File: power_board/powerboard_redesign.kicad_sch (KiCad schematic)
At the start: 18 parts, among them J1 282834-2, J2 282834-2, J3 282834-2, J4 282834-2, J5 BM06B-SRSS-TBLFSN, U1 PDQ30-Q24-D12-D

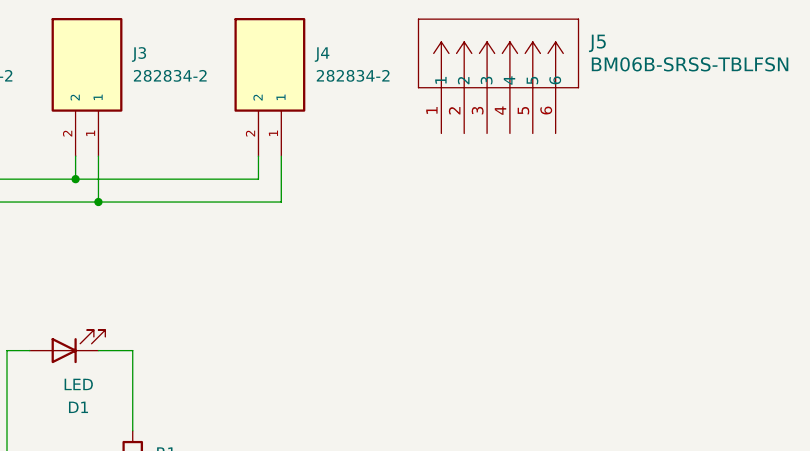
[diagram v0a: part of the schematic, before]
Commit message: Added connections to BM06B-SRSS-TB
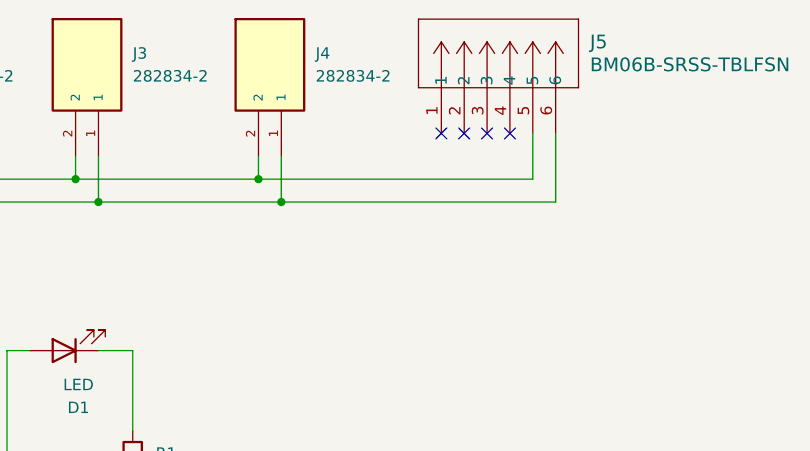
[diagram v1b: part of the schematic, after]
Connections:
- net at J5.5: now also C1.1, C4.1, C5.1, D1.2 (A), J2.2, J3.2, J4.2, U1.3 (+VOUT)
- net at J5.6: now also C1.2, C4.2, C5.2, J2.1, J3.1, J4.1, R1.2, U1.4 (COMMON)
- no-connect marks 3 -> 7
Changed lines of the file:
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@@
+	)
+	(junction
+		(at 223.52 58.42)
+		(diameter 0)
+		(color 0 0 0 0)
 	)
 	(junction
@@
 	)
 	(junction
+		(at 220.98 55.88)
+		(diameter 0)
+		(color 0 0 0 0)
+	)
+	(junction
 		(at 157.48 81.28)
 		(diameter 0)
@@
 	)
 	(no_connect
+		(at 246.38 50.8)
+	)
+	(no_connect
 		(at 157.48 93.98)
 	)
 	(no_connect
+		(at 248.92 50.8)
+	)
+	(no_connect
+		(at 241.3 50.8)
+	)
+	(no_connect
 		(at 83.82 86.36)
 	)
@@
 		(at 121.92 99.06)
 	)
+	(no_connect
+		(at 243.84 50.8)
+	)
 	(wire
 		(pts
@@
 	(wire
 		(pts
+			(xy 254 50.8) (xy 254 58.42)
+		)
+		(stroke
+			(width 0)
+			(type default)
+		)
+	)
+	(wire
+		(pts
+			(xy 223.52 58.42) (xy 254 58.42)
+		)
+		(stroke
+			(width 0)
+			(type default)
+		)
+	)
+	(wire
+		(pts
 			(xy 121.92 93.98) (xy 120.65 93.98)
 		)
@@
 	(wire
 		(pts
+			(xy 220.98 55.88) (xy 251.46 55.88)
+		)
+		(stroke
+			(width 0)
+			(type default)
+		)
+	)
+	(wire
+		(pts
 			(xy 203.2 53.34) (xy 203.2 58.42)
 		)
@@
 		)
 		(stroke
+			(width 0)
+			(type default)
+		)
+	)
+	(wire
+		(pts
+			(xy 251.46 50.8) (xy 251.46 55.88)
+		)
+		(stroke

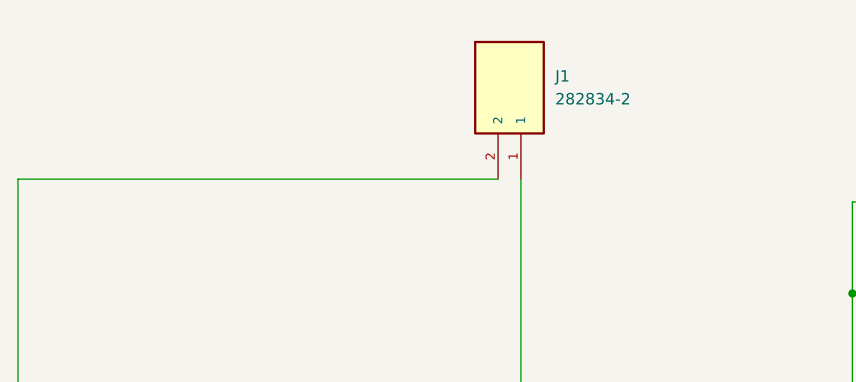
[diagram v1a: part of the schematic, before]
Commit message: Replaced Screw Terminal with B4B-XH-A for Battery
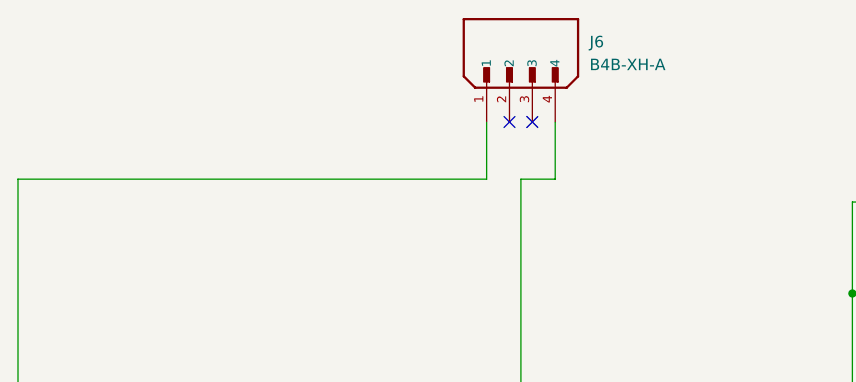
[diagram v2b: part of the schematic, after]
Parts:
- removed J1: 282834-2, F1TenthPowerBoard:TE_282834-2, symbol 282834-2:282834-2
- added J6: B4B-XH-A, F1TenthPowerBoard:JST_B4B-XH-A, symbol B4B-XH-A:B4B-XH-A
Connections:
- net at C2.2, C3.2, U1.2 (-VIN): now also J6.4
- net at S1.2: now also J6.1
- no-connect marks 7 -> 9
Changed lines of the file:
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@@
+	)
+	(no_connect
+		(at 119.38 49.53)
 	)
 	(no_connect
@@
 	)
 	(no_connect
+		(at 121.92 49.53)
+	)
+	(no_connect
 		(at 83.82 86.36)
 	)
@@
 	(wire
 		(pts
+			(xy 120.65 55.88) (xy 124.46 55.88)
+		)
+		(stroke
+			(width 0)
+			(type default)
+		)
+	)
+	(wire
+		(pts
 			(xy 120.65 55.88) (xy 120.65 93.98)
 		)
@@
 	(wire
 		(pts
+			(xy 64.77 55.88) (xy 116.84 55.88)
+		)
+		(stroke
+			(width 0)
+			(type default)
+		)
+	)
+	(wire
+		(pts
 			(xy 220.98 53.34) (xy 220.98 55.88)
 		)
@@
 	(wire
 		(pts
+			(xy 116.84 49.53) (xy 116.84 55.88)
+		)
+		(stroke
+			(width 0)
+			(type default)
+		)
+	)
+	(wire
+		(pts
 			(xy 110.49 106.68) (xy 120.65 106.68)
 		)
@@
 	(wire
 		(pts
-			(xy 64.77 55.88) (xy 118.11 55.88)
-		)
-		(stroke
-			(width 0)
-			(type default)
-		)
-	)
-	(wire
-		(pts
 			(xy 223.52 58.42) (xy 203.2 58.42)
 		)
@@
 		(pts
 			(xy 170.18 93.98) (xy 193.04 93.98)
+		)
+		(stroke
+			(width 0)
+			(type default)
+		)
+	)
+	(wire
+		(pts
+			(xy 124.46 49.53) (xy 124.46 55.88)
 		)
 		(stroke
@@
 	)
 	(symbol
+		(lib_id "B4B-XH-A:B4B-XH-A")
+		(at 119.38 41.91 90)
+		(unit 1)
+		(exclude_from_sim no)
+		(in_bom yes)
+		(on_board yes)
+		(dnp no)
+		(fields_autoplaced yes)
+		(property "Reference" "J6"
+			(at 128.27 40.6399 90)
+			(effects
+				(font
+					(size 1.27 1.27)
+				)
+				(justify right)
+			)
+		)
+		(property "Value" "B4B-XH-A"
+			(at 128.27 43.1799 90)
+			(effects
+				(font
+					(size 1.27 1.27)
+				)
+				(justify right)
+			)
+		)
+		(property "Footprint" "F1TenthPowerBoard:JST_B4B-XH-A"
+			(at 119.38 41.91 0)
+			(effects
+				(font
+					(size 1.27 1.27)
+				)
+				(justify bottom)
+				(hide yes)
+			)
+		)
+		(property "Datasheet" "https://www.jst-mfg.com/product/pdf/eng/eXH.pdf"
+			(at 119.38 41.91 0)
+			(effects
+				(font
+					(size 1.27 1.27)
+				)
+				(hide yes)
+			)
+		)
+		(property "Description" "Battery Connector"
+			(at 119.38 41.91 0)
+			(effects
+				(font
+					(size 1.27 1.27)
+				)
+				(hide yes)
+			)
+		)
+		(property "PARTREV" "7/4/21"
+			(at 119.38 41.91 0)
+			(effects
+				(font
+					(size 1.27 1.27)
+				)
+				(justify bottom)
+				(hide yes)
+			)
+		)
+		(property "STANDARD" "Manufacturer Recommendations"
+			(at 119.38 41.91 0)
+			(effects
+				(font
+					(size 1.27 1.27)
+				)
+				(justify bottom)
+				(hide yes)
+			)
+		)
+		(property "MAXIMUM_PACKAGE_HEIGHT" "7.00 mm"
+			(at 119.38 41.91 0)
+			(effects
+				(font
+					(size 1.27 1.27)
+				)
+				(justify bottom)
+				(hide yes)
+			)
+		)
+		(property "MANUFACTURER" "JST"
+			(at 119.38 41.91 0)
+			(effects
+				(font
+					(size 1.27 1.27)
+				)
+				(justify bottom)
+				(hide yes)
+			)
+		)
+		(pin "3"
+		)
+		(pin "1"
+		)
+		(pin "2"
+		)
+		(pin "4"
+		)
+		(instances
+			(project ""
+				(path "/730a7e3b-debe-415e-92d1-0c8950d2c05d"
+					(reference "J6")
+					(unit 1)
+				)
+			)
+		)
+	)
+	(symbol
 		(lib_id "Device:LED")
 		(at 199.39 74.93 180)
@@
 					(unit 1)
 				)
-			)
-		)
-	)
-	(symbol
-		(lib_id "282834-2:282834-2")
-		(at 118.11 48.26 270)
-		(unit 1)
-		(exclude_from_sim no)
-		(in_bom yes)
-		(on_board yes)
-		(dnp no)
-		(fields_autoplaced yes)
-		(property "Reference" "J1"
-			(at 124.46 44.4499 90)
-			(effects
-				(font
-					(size 1.27 1.27)
-				)
-				(justify left)
-			)
-		)
-		(property "Value" "282834-2"
-			(at 124.46 46.9899 90)
-			(effects
-				(font
-					(size 1.27 1.27)
-				)
-				(justify left)
-			)
-		)
-		(property "Footprint" "F1TenthPowerBoard:TE_282834-2"
-			(at 118.11 48.26 0)
-			(effects
-				(font
-					(size 1.27 1.27)
-				)
-				(justify bottom)
-				(hide yes)
-			)
-		)
-		(property "Datasheet" "https://www.snapeda.com/parts/282834-2/TE%20Connectivity/datasheet/"
-			(at 118.11 48.26 0)
-			(effects
-				(font
-					(size 1.27 1.27)
-				)
-				(hide yes)
-			)
-		)
-		(property "Description" "Terminal Block Connector PCB 2.54 mm 30-16 AWG Green 10 A 150 V M1.6 | TE Connectivity 282834-2"
-			(at 118.11 48.26 0)
-			(effects
-				(font
-					(size 1.27 1.27)
-				)
-				(hide yes)
-			)
-		)
-		(property "Comment" "282834-2"
-			(at 118.11 48.26 0)
-			(effects
-				(font
-					(size 1.27 1.27)
-				)
-				(justify bottom)
-				(hide yes)
-			)
-		)
-		(property "MF" "TE Connectivity"
-			(at 118.11 48.26 0)
-			(effects
-				(font
-					(size 1.27 1.27)
-				)
-				(justify bottom)
-				(hide yes)
-			)
-		)
-		(property "MAXIMUM_PACKAGE_HEIGHT" "10 mm"
-			(at 118.11 48.26 0)
-			(effects
-				(font
-					(size 1.27 1.27)
-				)
-				(justify bottom)
-				(hide yes)
-			)
-		)
-		(property "Package" "None"
-			(at 118.11 48.26 0)
-			(effects
-				(font
-					(size 1.27 1.27)
-				)
-				(justify bottom)
-				(hide yes)
-			)
-		)
-		(property "Price" "None"
-			(at 118.11 48.26 0)
-			(effects
-				(font
-					(size 1.27 1.27)
-				)
-				(justify bottom)
-				(hide yes)
-			)
-		)
-		(property "Check_prices" "https://www.snapeda.com/parts/282834-2/TE+Connectivity+AMP+Connectors/view-part/?ref=eda"
-			(at 118.11 48.26 0)
-			(effects
-				(font
-					(size 1.27 1.27)
-				)
-				(justify bottom)
-				(hide yes)
-			)
-		)
-		(property "STANDARD" "Manufacturer Recommendations"
-			(at 118.11 48.26 0)
-			(effects
-				(font
-					(size 1.27 1.27)
-				)
-				(justify bottom)
-				(hide yes)
-			)
-		)
-		(property "PARTREV" "D"
-			(at 118.11 48.26 0)
-			(effects
-				(font
-					(size 1.27 1.27)
-				)
-				(justify bottom)
-				(hide yes)
-			)
-		)
-		(property "SnapEDA_Link" "https://www.snapeda.com/parts/282834-2/TE+Connectivity+AMP+Connectors/view-part/?ref=snap"
-			(at 118.11 48.26 0)
-			(effects
-				(font
-					(size 1.27 1.27)
-				)
-				(justify bottom)
-				(hide yes)
-			)
-		)
-		(property "MP" "282834-2"
-			(at 118.11 48.26 0)
-			(effects
-				(font
-					(size 1.27 1.27)
-				)
-				(justify bottom)
-				(hide yes)
-			)
-		)
-		(property "EU_RoHS_Compliance" "Compliant with Exemptions"
-			(at 118.11 48.26 0)
-			(effects
-				(font
-					(size 1.27 1.27)
-				)
-				(justify bottom)
-				(hide yes)
-			)
-		)
-		(property "Description_1" "Terminal Block Connector PCB 2.54 mm 30-16 AWG Green 10 A 150 V M1.6 | TE Connectivity 282834-2"
-			(at 118.11 48.26 0)
-			(effects
-				(font
-					(size 1.27 1.27)
-				)
-				(justify bottom)
-				(hide yes)
-			)
-		)
-		(property "MANUFACTURER" "TE Connectivity"
-			(at 118.11 48.26 0)
-			(effects
-				(font
-					(size 1.27 1.27)
-				)
-				(justify bottom)
-				(hide yes)
-			)
-		)
-		(property "Availability" "In Stock"
-			(at 118.11 48.26 0)
-			(effects
-				(font
-					(size 1.27 1.27)
-				)
-				(justify bottom)
-				(hide yes)
-			)
-		)
-		(property "SNAPEDA_PN" "282834-2"
-			(at 118.11 48.26 0)
-			(effects
-				(font
-					(size 1.27 1.27)
-				)
-				(justify bottom)
-				(hide yes)
-			)
-		)
-		(pin "2"
-		)
-		(pin "1"
-		)
-		(instances
-			(project ""
-				(path "/730a7e3b-debe-415e-92d1-0c8950d2c05d"
-					(reference "J1")
-					(unit 1)
-				)

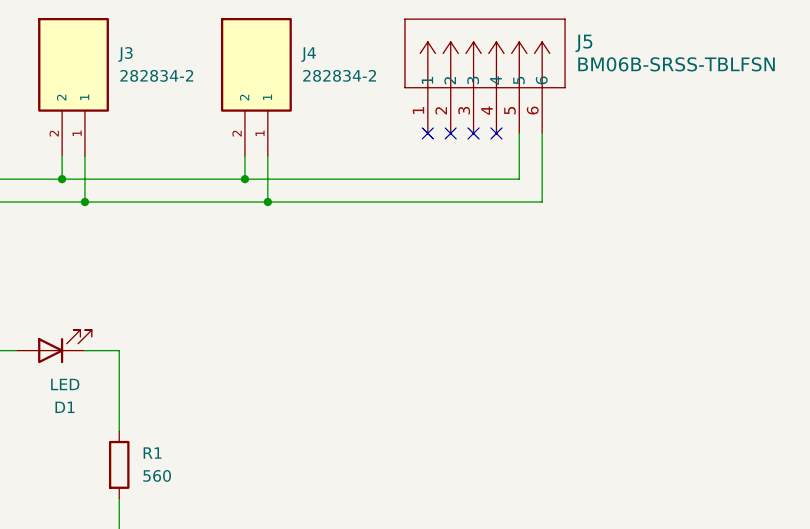
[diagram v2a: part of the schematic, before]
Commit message: Updated schematic and PCB for V3
Added 4-pin connector for LiDAR connector
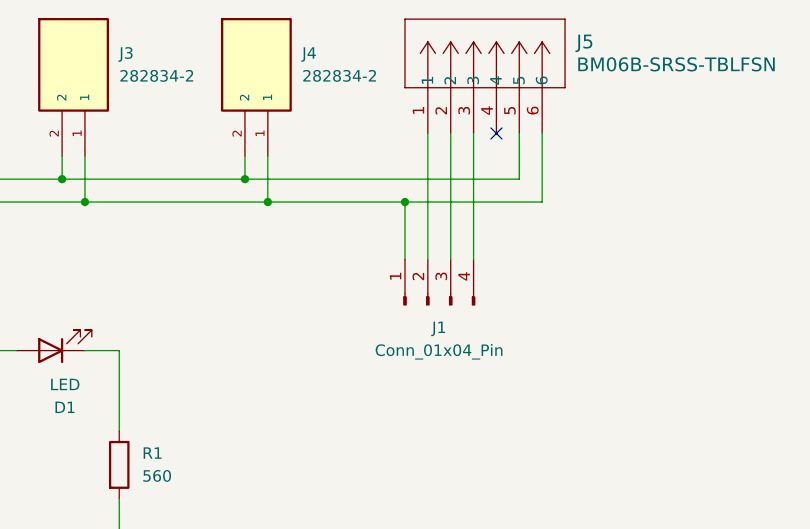
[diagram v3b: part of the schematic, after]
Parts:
- added J1: Conn_01x04_Pin, Connector_PinHeader_2.54mm:PinHeader_1x04_P2.54mm_Vertical, symbol Connector:Conn_01x04_Pin
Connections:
- net at J5.1: now also J1.2 (Pin_2)
- net at J5.2: now also J1.3 (Pin_3)
- net at J5.3: now also J1.4 (Pin_4)
- net at C1.2, C4.2, C5.2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: now also J1.1 (Pin_1)
- no-connect marks 9 -> 6
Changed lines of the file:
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@@
+	)
+	(junction
+		(at 238.76 58.42)
+		(diameter 0)
+		(color 0 0 0 0)
 	)
 	(junction
@@
 	)
 	(no_connect
-		(at 246.38 50.8)
+		(at 248.92 50.8)
 	)
 	(no_connect
@@
 	)
 	(no_connect
-		(at 248.92 50.8)
-	)
-	(no_connect
-		(at 241.3 50.8)
-	)
-	(no_connect
 		(at 121.92 49.53)
 	)
@@
 		(at 121.92 99.06)
 	)
-	(no_connect
-		(at 243.84 50.8)
-	)
 	(wire
 		(pts
@@
 	(wire
 		(pts
-			(xy 223.52 58.42) (xy 254 58.42)
-		)
-		(stroke
-			(width 0)
-			(type default)
-		)
-	)
-	(wire
-		(pts
 			(xy 121.92 93.98) (xy 120.65 93.98)
 		)
@@
 	(wire
 		(pts
+			(xy 241.3 50.8) (xy 241.3 64.77)
+		)
+		(stroke
+			(width 0)
+			(type default)
+		)
+	)
+	(wire
+		(pts
 			(xy 83.82 91.44) (xy 102.87 91.44)
 		)
@@
 	(wire
 		(pts
+			(xy 238.76 58.42) (xy 254 58.42)
+		)
+		(stroke
+			(width 0)
+			(type default)
+		)
+	)
+	(wire
+		(pts
 			(xy 223.52 58.42) (xy 203.2 58.42)
 		)
@@
 	(wire
 		(pts
+			(xy 223.52 58.42) (xy 238.76 58.42)
+		)
+		(stroke
+			(width 0)
+			(type default)
+		)
+	)
+	(wire
+		(pts
 			(xy 200.66 55.88) (xy 220.98 55.88)
 		)
@@
 	(wire
 		(pts
+			(xy 243.84 50.8) (xy 243.84 64.77)
+		)
+		(stroke
+			(width 0)
+			(type default)
+		)
+	)
+	(wire
+		(pts
 			(xy 102.87 91.44) (xy 121.92 91.44)
 		)
@@
 	(wire
 		(pts
+			(xy 238.76 58.42) (xy 238.76 64.77)
+		)
+		(stroke
+			(width 0)
+			(type default)
+		)
+	)
+	(wire
+		(pts
 			(xy 157.48 85.09) (xy 162.56 85.09)
 		)
@@
 		(pts
 			(xy 181.61 53.34) (xy 181.61 58.42)
+		)
+		(stroke
+			(width 0)
+			(type default)
+		)
+	)
+	(wire
+		(pts
+			(xy 246.38 50.8) (xy 246.38 64.77)
 		)
 		(stroke
@@
 					(unit 1)
 				)
+			)
+		)
+	)
+	(symbol
+		(lib_id "Connector:Conn_01x04_Pin")
+		(at 241.3 69.85 90)
+		(unit 1)
+		(exclude_from_sim no)
+		(in_bom yes)
+		(on_board yes)
+		(dnp no)
+		(fields_autoplaced yes)
+		(property "Reference" "J1"
+			(at 242.57 72.39 90)
+			(effects
+				(font
+					(size 1.27 1.27)
+				)
+			)
+		)
+		(property "Value" "Conn_01x04_Pin"
+			(at 242.57 74.93 90)
+			(effects
+				(font
+					(size 1.27 1.27)
+				)
+			)
+		)
+		(property "Footprint" "Connector_PinHeader_2.54mm:PinHeader_1x04_P2.54mm_Vertical"
+			(at 241.3 69.85 0)
+			(effects
+				(font
+					(size 1.27 1.27)
+				)
+				(hide yes)
+			)
+		)
+		(property "Datasheet" "~"
+			(at 241.3 69.85 0)
+			(effects
+				(font
+					(size 1.27 1.27)
+				)
+				(hide yes)
+			)
+		)
+		(property "Description" "Generic connector, single row, 01x04, script generated"
+			(at 241.3 69.85 0)
+			(effects
+				(font
+					(size 1.27 1.27)
+				)
+				(hide yes)
+			)
+		)
+		(pin "2"
+		)
+		(pin "3"
+		)
+		(pin "1"
+		)
+		(pin "4"
+		)
+		(instances
+			(project ""
+				(path "/730a7e3b-debe-415e-92d1-0c8950d2c05d"
+					(reference "J1")
+					(unit 1)
+				)

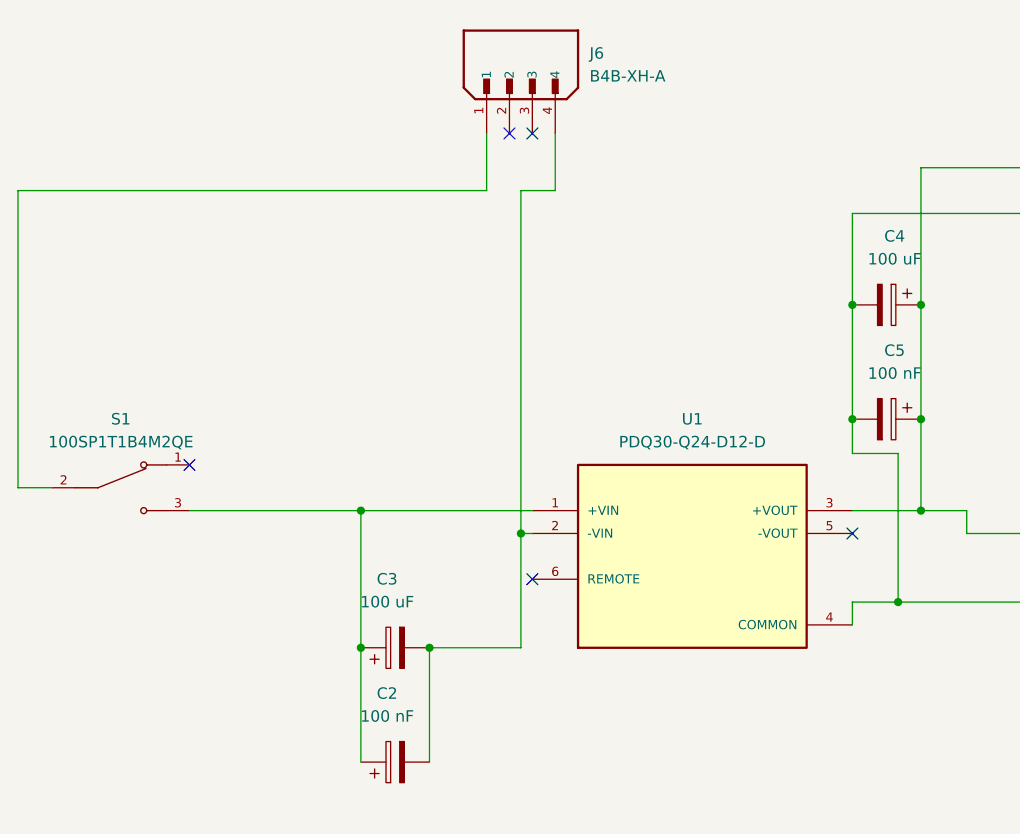
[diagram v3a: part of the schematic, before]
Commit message: Updated Powerboard to have S12 instead of D12 + Added 2 Terminal Block on Battery Side
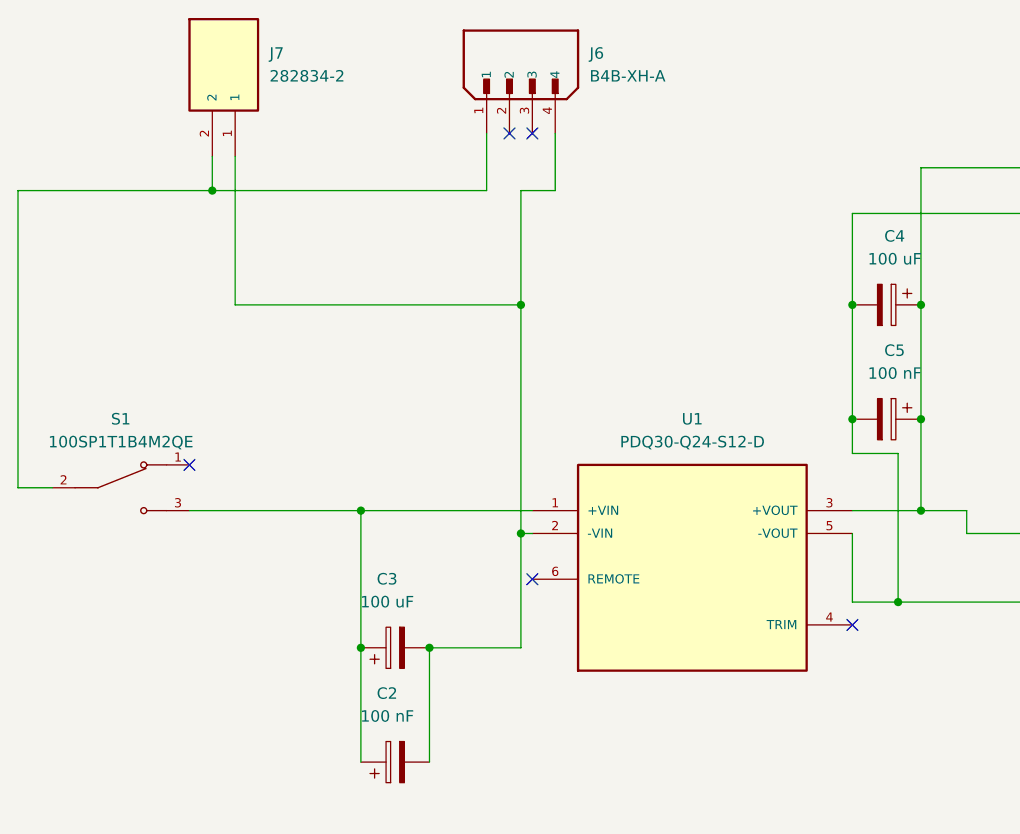
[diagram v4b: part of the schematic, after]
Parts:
- removed U1: PDQ30-Q24-D12-D, F1TenthPowerBoard:CONV_PDQ30-Q24-D12-D, symbol PDQ30-Q24-D12-D:PDQ30-Q24-D12-D
- added J7: 282834-2, F1TenthPowerBoard:TE_282834-2, symbol 282834-2:282834-2
- added U1: PDQ30-Q24-S12-D, F1TenthPowerBoard:CONV_PDQ30-Q24-S12-D, symbol PDQ30-Q24-S12-D:PDQ30-Q24-S12-D
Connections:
- net at C1.1, C4.1, C5.1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: now also U1.3 (+VOUT)
- net at C1.2, C4.2, C5.2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: now also U1.5 (-VOUT)
- net at J6.1, S1.2: now also J7.2
- net at C2.2, C3.2, J6.4: now also J7.1, U1.2 (-VIN)
- net at C2.1, C3.1, S1.3: now also U1.1 (+VIN)
